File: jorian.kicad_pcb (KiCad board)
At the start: 2 copper layers, 98.9 x 100 mm, 90 parts, among them J6 lipo_charger, U3 LP3990-3.3v

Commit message: reroute take 3, moved a bit by hand
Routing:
- net /S20_B: track 32.5 -> 99.3 mm, vias 0 -> 6
- net /S4: track 72.6 -> 118.2 mm, vias 1 -> 11
- net BAT-: track 63.8 -> 100.2 mm, vias 2 -> 4
- net BAT+: track 48.5 -> 79.4 mm
- net OUT+: track 65.3 -> 94.9 mm, vias 1 -> 6
- net /GND_B: track 216.0 -> 244.3 mm, vias 5 -> 4
- net Net-(J6-Pad4): track 32.8 -> 60.9 mm, vias 1 -> 7
- net VCC: track 611.7 -> 635.6 mm
- net /S19: track 128.2 -> 105.7 mm, vias 4 -> 5
- net LIPO+: track 35.8 -> 56.7 mm, vias 3 -> 6
- net /DIN21_B: track 18.1 -> 38.1 mm
- net SCL: track 90.9 -> 71.4 mm, vias 6 -> 5
- net Net-(L12-Pad3): track 44.0 -> 62.9 mm, vias 3 -> 4
- net /VCC_B: track 139.9 -> 122.5 mm, vias 4 -> 7
- net /S7: track 55.6 -> 72.8 mm, vias 1 -> 6
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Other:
- outline, holes or cut-outs redrawn

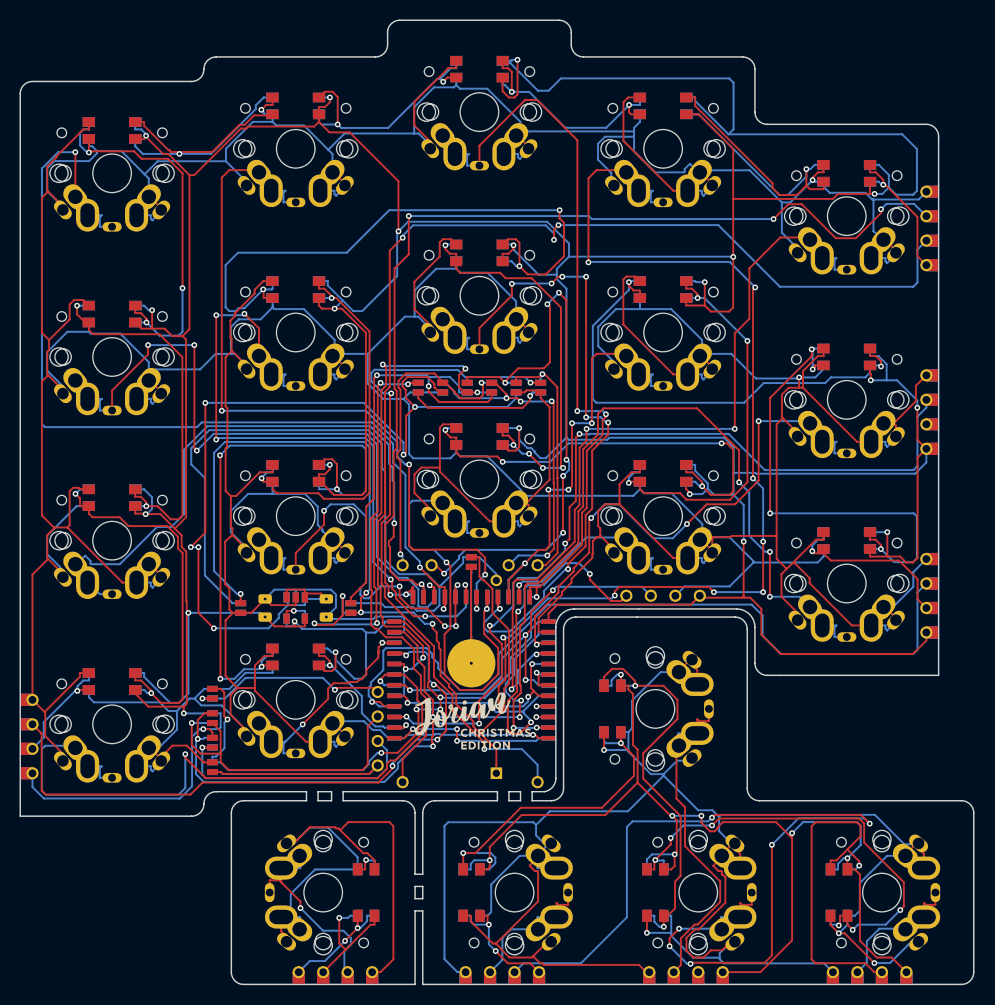
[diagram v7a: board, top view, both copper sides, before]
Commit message: fixed li-po charger jumpers on the back side
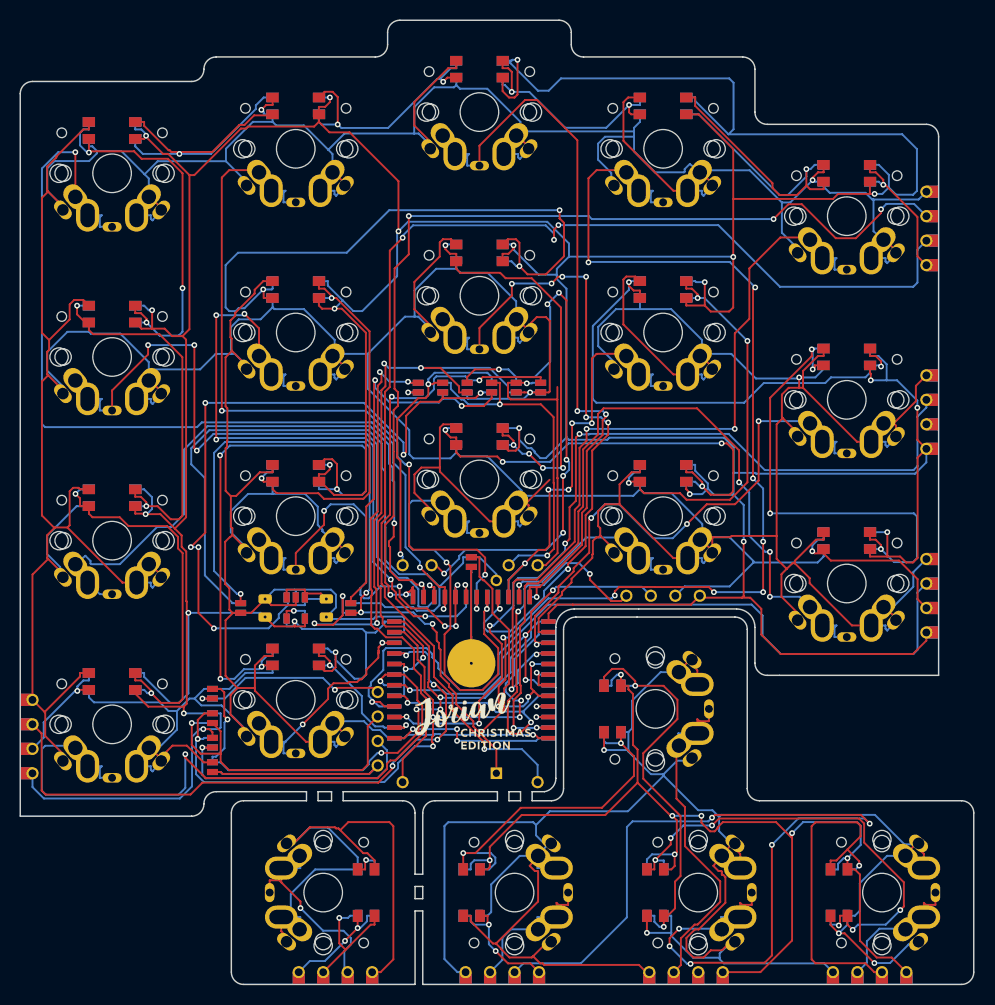
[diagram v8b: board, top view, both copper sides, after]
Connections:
- JP22 pad 1: VUSB -> GND
- JP23 pad 1: GND -> LIPO-
- JP24 pad 1: OUT+ -> LIPO+
- JP25 pad 1: LIPO+ -> OUT+
- JP26 pad 1: LIPO- -> GND
- JP27 pad 1: GND -> VUSB
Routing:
- net VUSB: track 14.7 -> 2.10 mm
- net OUT+: track 94.9 -> 84.2 mm
- net LIPO+: track 56.7 -> 63.7 mm, vias 6 -> 5
- net GND: track 990.4 -> 995.1 mm, vias 4 -> 5
- net LIPO-: track 44.5 -> 40.0 mm
- net Net-(J6-Pad2): track 72.0 -> 68.1 mm
- net Net-(J6-Pad6): track 26.3 -> 29.9 mm
- net Net-(J6-Pad3): track 32.4 -> 30.5 mm
- net Net-(J6-Pad1): track 51.6 -> 53.2 mm
- net VCC: track 635.6 -> 636.3 mm
- net Net-(J6-Pad5): vias 4 -> 2
